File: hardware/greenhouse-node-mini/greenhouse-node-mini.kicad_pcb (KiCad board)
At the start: 4 copper layers, 70 x 50 mm, 43 parts, among them J1 Molex_KK_396_1x2, J2 JST_XH_2.54mm_1x2, J4 Molex_KK_396_1x2, J5 JST_XH_2.54mm_1x4, J6 PinHeader_1x04_P2.54mm, J7 PinHeader_1x04_P2.54mm, Q1 A42, SW1 SW_Push, U1 ATtiny84A-P, U2 L7805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

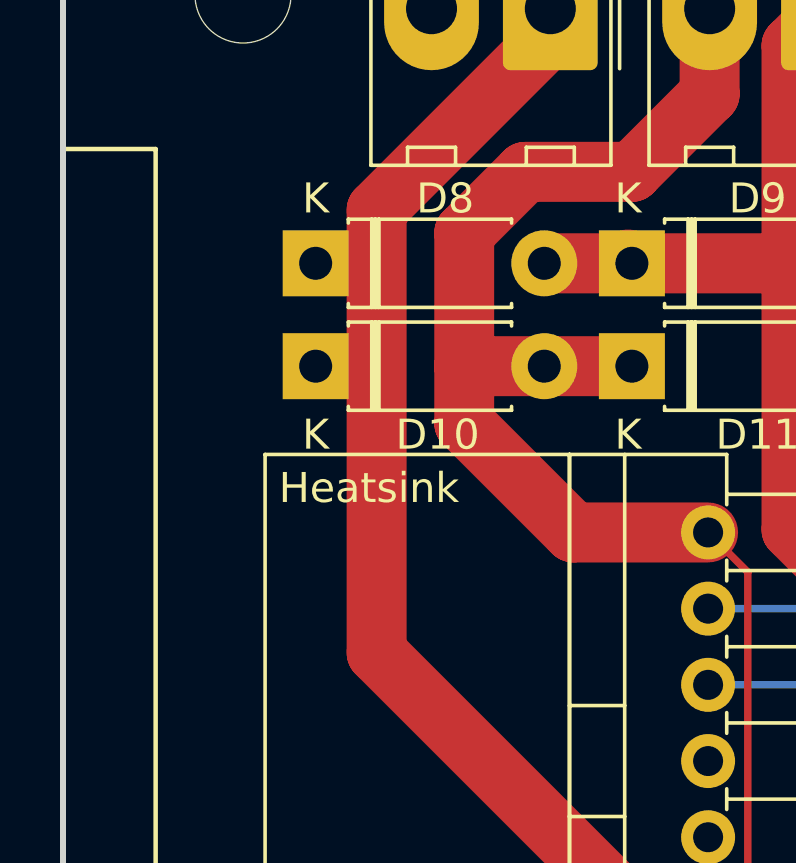
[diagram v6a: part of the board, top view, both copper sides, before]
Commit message: Add hidden 10V track for D8+D10
Not sure if necessary
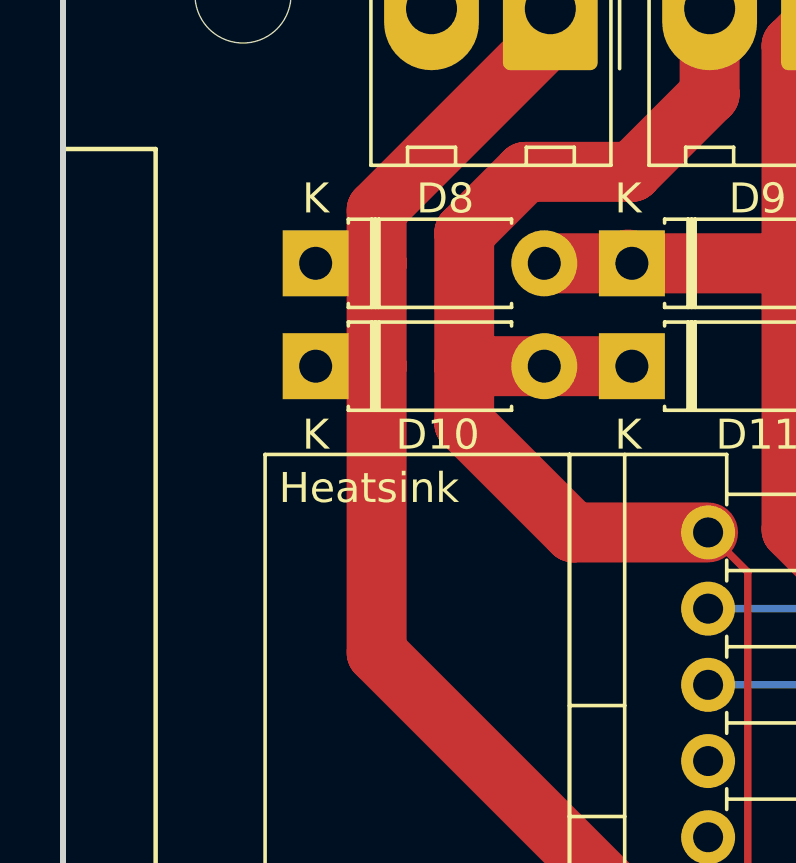
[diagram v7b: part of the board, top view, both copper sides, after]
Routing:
- net +10V: track 52.4 -> 56.4 mm
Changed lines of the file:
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@@
   (segment (start 123.317 59.309) (end 124.714 60.706) (width 0.25) (layer "F.Cu") (net 4))
   (segment (start 121.285 56.901) (end 121.285 58.6105) (width 0.25) (layer "F.Cu") (net 4))
+  (segment (start 76.454 55.372) (end 76.454 64.9224) (width 2) (layer "F.Cu") (net 5))
+  (segment (start 74.422 55.372) (end 76.454 55.372) (width 2) (layer "F.Cu") (net 5))
+  (segment (start 76.454 51.943) (end 76.454 55.372) (width 2) (layer "F.Cu") (net 5))
+  (segment (start 74.422 51.943) (end 76.454 51.943) (width 2) (layer "F.Cu") (net 5))
+  (segment (start 76.454 50.165909) (end 76.454 51.943) (width 2) (layer "F.Cu") (net 5))
   (segment (start 82.244 44.375909) (end 76.454 50.165909) (width 2) (layer "F.Cu") (net 5))
   (segment (start 85.1458 73.6142) (end 87.503 73.6142) (width 2) (layer "F.Cu") (net 5))
   (segment (start 95.758 40.386) (end 85.314 40.386) (width 0.5) (layer "F.Cu") (net 5))
   (segment (start 76.454 64.9224) (end 85.1458 73.6142) (width 2) (layer "F.Cu") (net 5))
-  (segment (start 76.454 50.165909) (end 76.454 64.9224) (width 2) (layer "F.Cu") (net 5))
   (segment (start 85.314 40.386) (end 82.244 43.456) (width 0.5) (layer "F.Cu") (net 5))
   (segment (start 113.284 72.263) (end 112.259489 71.238489) (width 0.25) (layer "F.Cu") (net 6))
